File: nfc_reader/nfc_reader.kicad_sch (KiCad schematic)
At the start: 2 parts

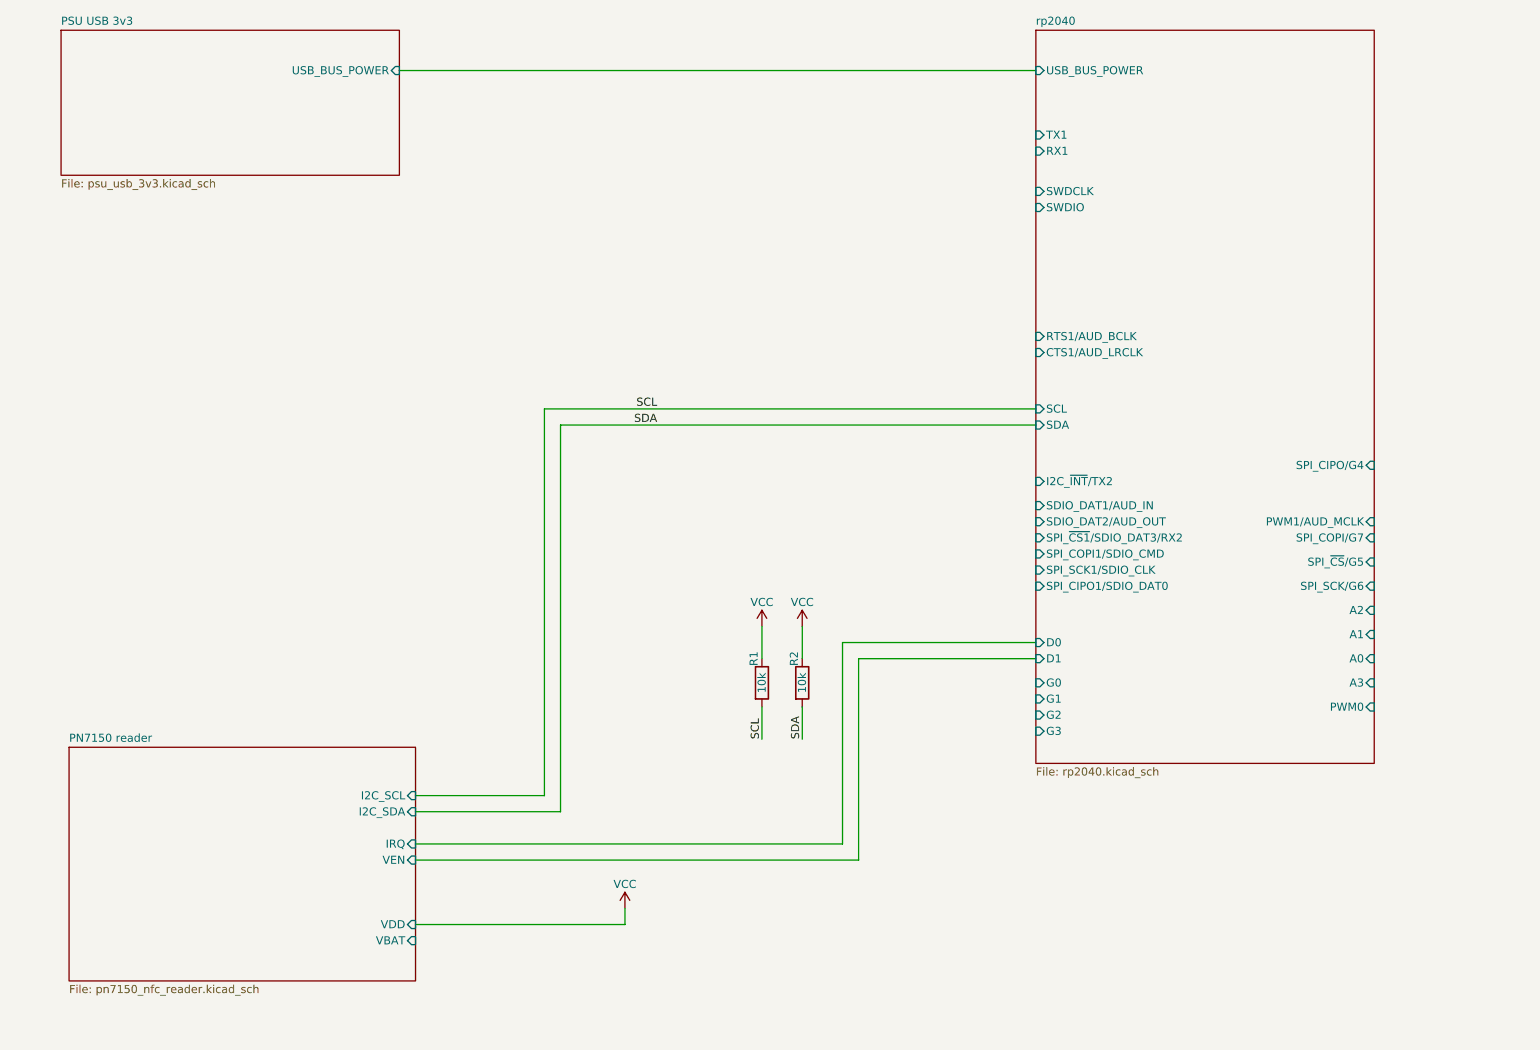
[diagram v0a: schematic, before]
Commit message: Added front artwork to nfc_reader
Also
- Fixed error with missing power to PN7150 radio
- Added two buttons and two LEDs
- Moved things around a little
- Updated BOM and created pos file
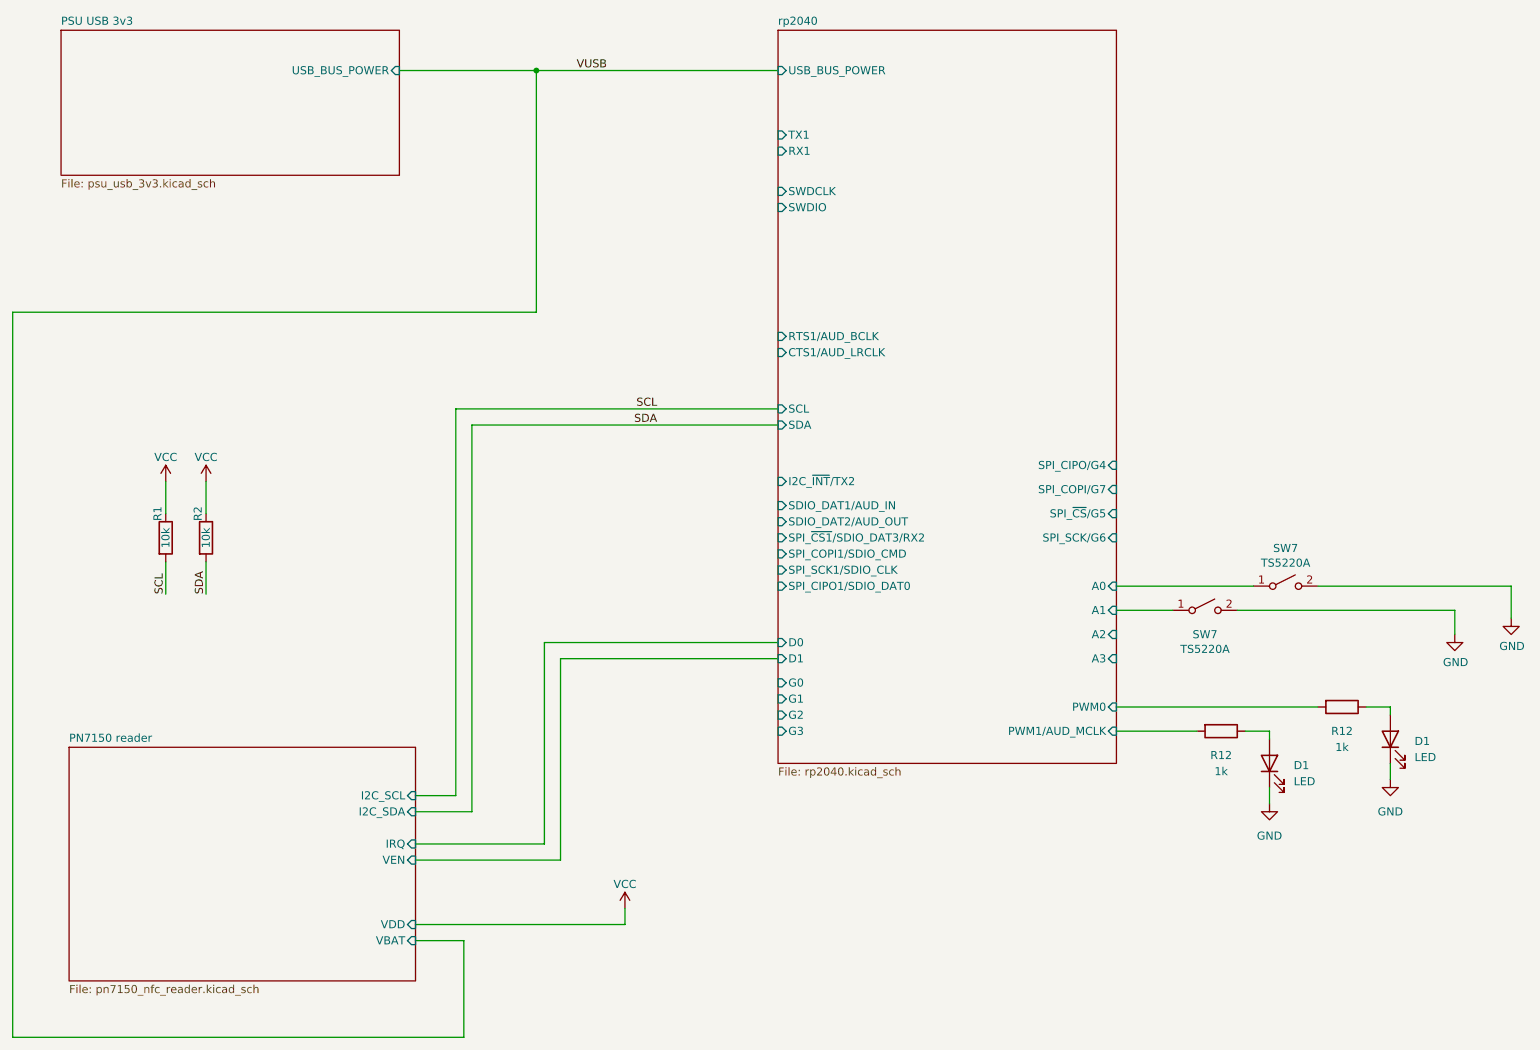
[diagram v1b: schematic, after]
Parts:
- added D1 (x2): LED, LED_SMD:LED_0603_1608Metric, symbol Device:LED
- added R12 (x2): 1k, Resistor_SMD:R_0603_1608Metric, symbol Device:R
- added SW7 (x2): TS5220A, Button_Switch_SMD:SW_SPST_TL3342, symbol Switch:SW_SPST
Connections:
- net rp2040/A0: now also SW7.1 (A)
- net rp2040/A1: now also SW7.1 (A)
- net rp2040/PWM0: now also R12.2
- net rp2040/PWM1/AUD_MCLK: now also R12.2
- new net: D1.2 (A), R12.1 (x2)
- new net GND: D1.1 (K), D1.1 (K), SW7.2 (B), SW7.2 (B)
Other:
- moved on the sheet: R1, R2
